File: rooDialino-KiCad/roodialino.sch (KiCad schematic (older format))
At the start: 47 parts, among them J1 Raspi Connector, J2 ICSP, J3 FTDI, J4 IR Receiver, J5 IR LED, Q1 2N7002, Q2 2N7002, Q3 2N7002, SW1 SW_Push, U1 ATmega328P, U2 TSOP312xx, U3 TXS0108EPW, Y1 16 MHz

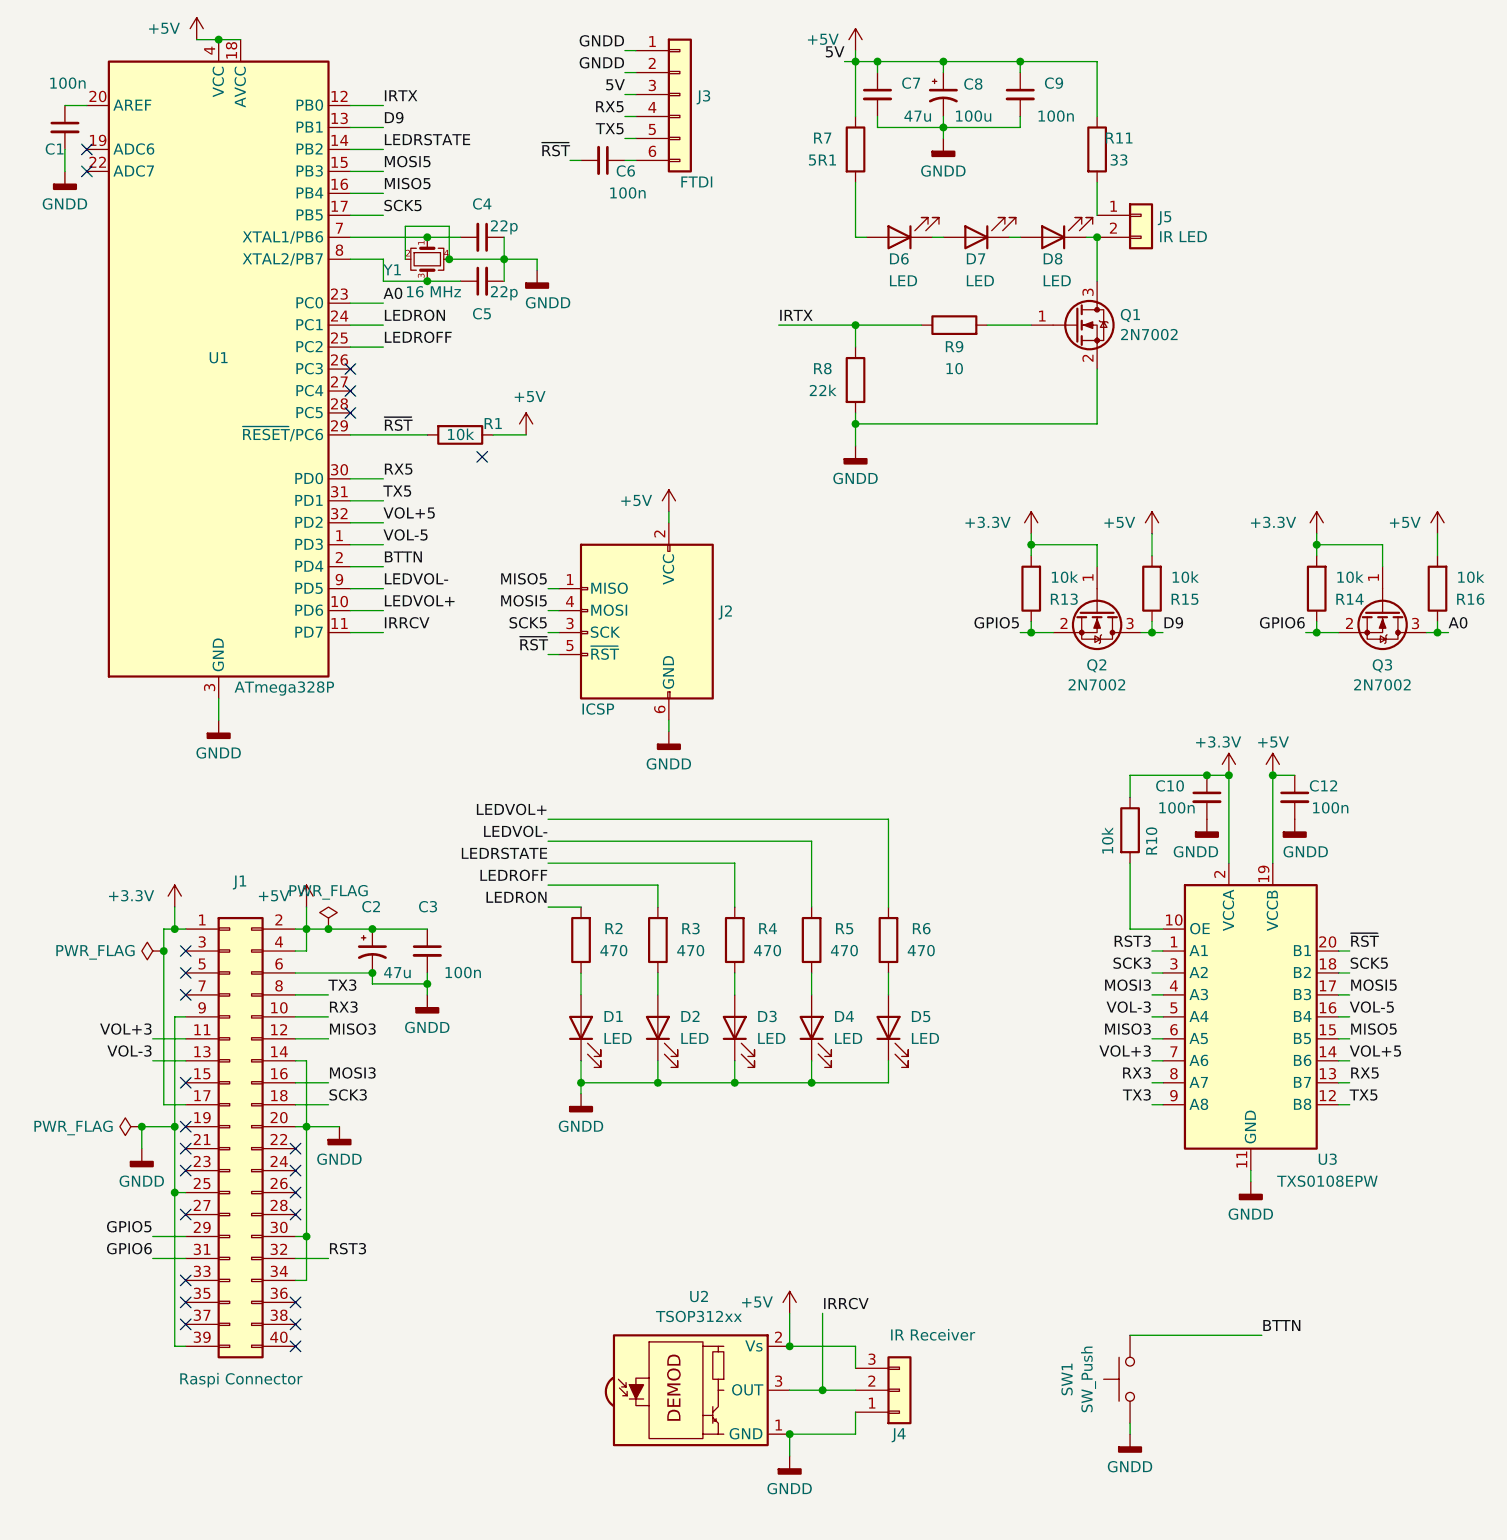
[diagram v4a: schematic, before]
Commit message: Fixing IRX wiring, adding ESO protection
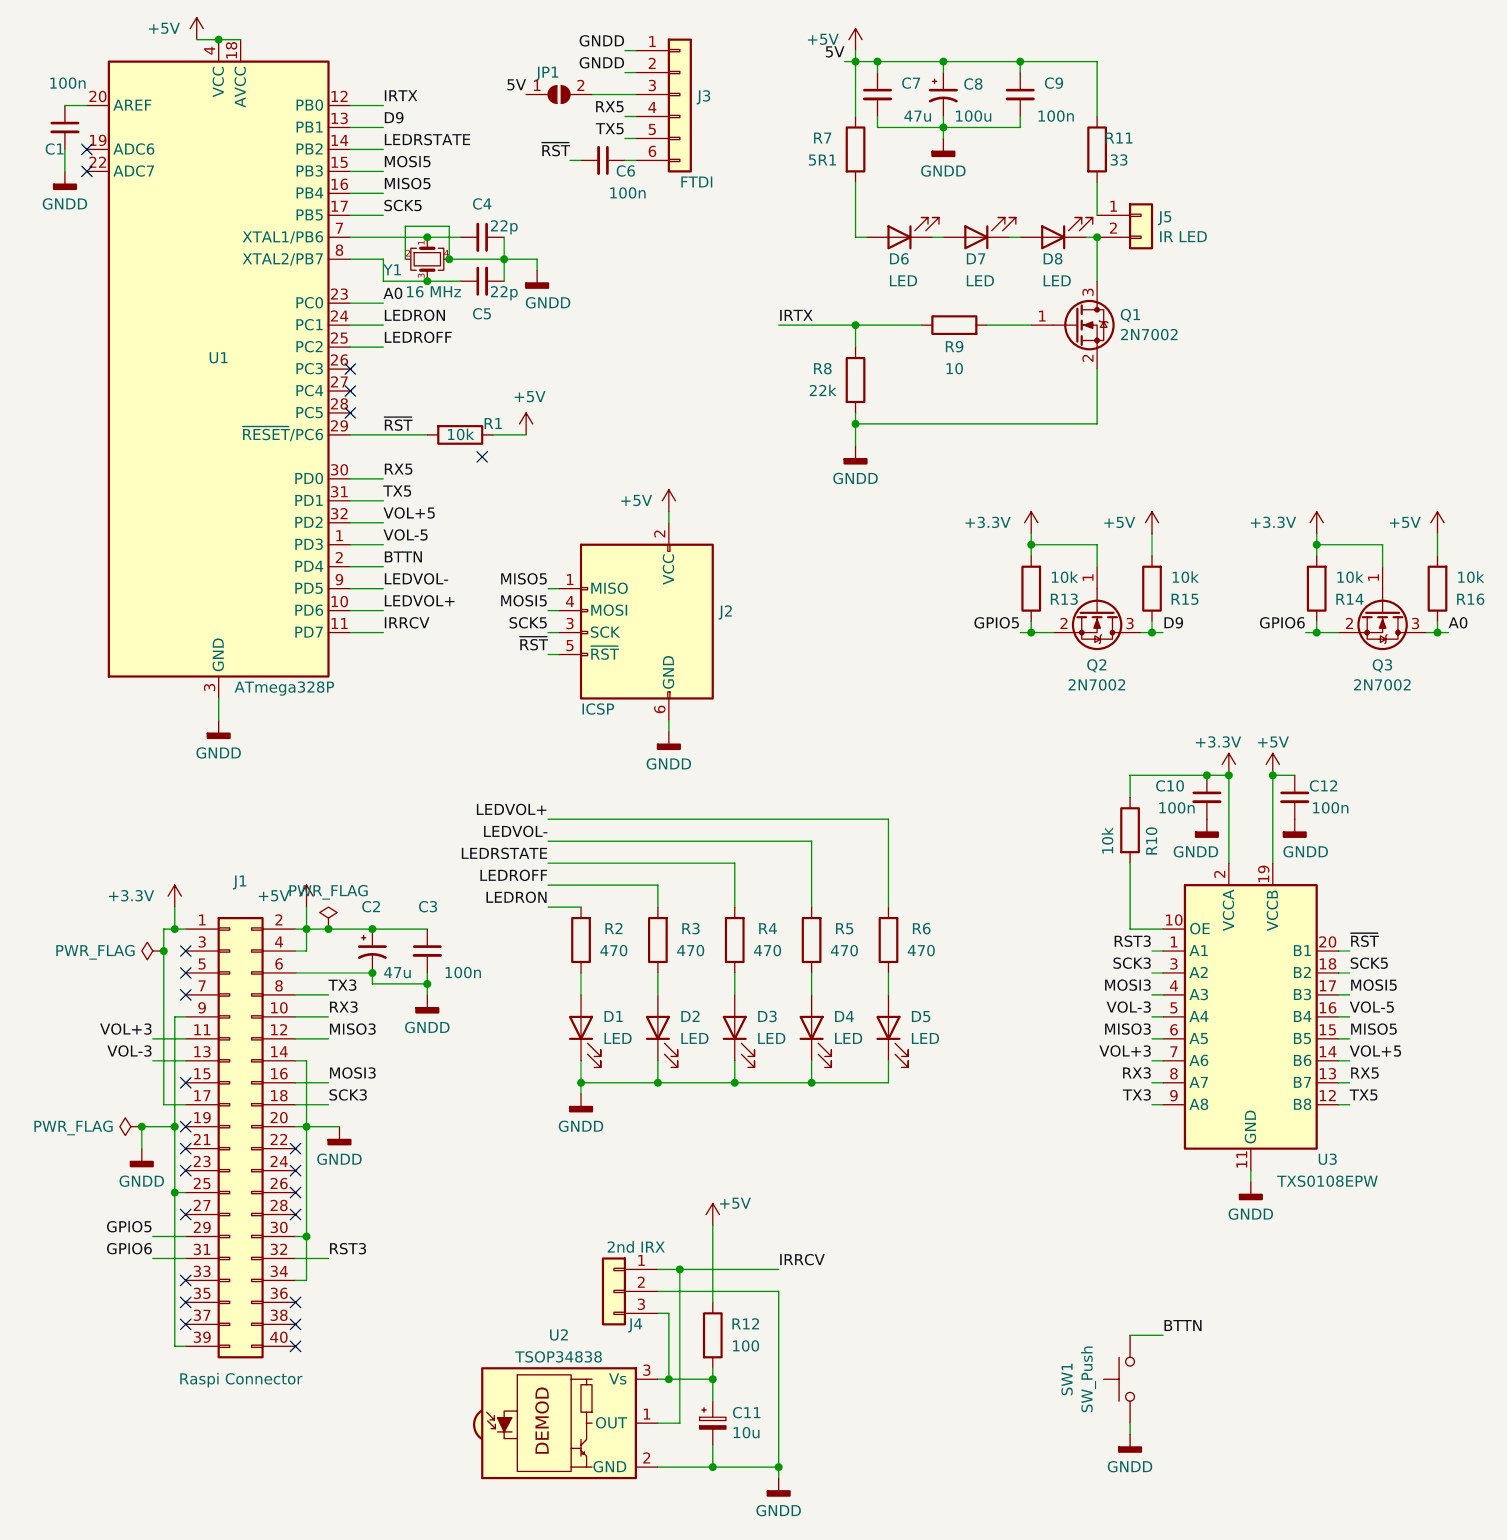
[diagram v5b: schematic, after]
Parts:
- removed U2: TSOP312xx, OptoDevice:Vishay_MINICAST-3Pin, symbol Interface_Optical:TSOP312xx
- added C11: 10u, Capacitor_Tantalum_SMD:CP_EIA-3216-18_Kemet-A, symbol Device:CP_Small
- added JP1: SolderJumper_2_Open, symbol Jumper:SolderJumper_2_Open
- added R12: 100, Resistor_SMD:R_0805_2012Metric, symbol Device:R
- added U2: TSOP34838, OptoDevice:Vishay_MOLD-3Pin, symbol Interface_Optical:TSOP348xx
- J4: value IR Receiver -> 2nd IRX
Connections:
- net +5V: now also JP1.1 (A), R12.1; no longer J3.3 (Pin_3), J4.3 (Pin_3)
- net GNDD: now also J4.2 (Pin_2), C11.2, U2.2 (GND); no longer J4.1 (Pin_1)
- net IRRCV: now also J4.1 (Pin_1), U2.1 (OUT); no longer J4.2 (Pin_2)
- new net: J3.3 (Pin_3), JP1.2 (B)
- new net: C11.1, J4.3 (Pin_3), R12.2, U2.3 (Vs)
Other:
- moved on the sheet: J4
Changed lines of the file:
@@
 Text Label 3250 950  2    50   ~ 0
 GNDD
-Text Label 3250 1050 2    50   ~ 0
+Text Label 2800 1050 2    50   ~ 0
 5V
 Text Label 3250 1150 2    50   ~ 0
@@
 	3250 1150 3300 1150
 Wire Wire Line
-	3250 1050 3300 1050
+	3100 1050 3300 1050
 Wire Wire Line
 	3250 950  3300 950
@@
 Connection ~ 5050 900
 $Comp
-L Interface_Optical:TSOP312xx U2
-U 1 1 61922DF7
-P 3600 6950
-F 0 "U2" H 3588 7375 50  0000 C CNN
-F 1 "TSOP312xx" H 3588 7284 50  0000 C CNN
-F 2 "OptoDevice:Vishay_MINICAST-3Pin" H 3550 6575 50  0001 C CNN
-F 3 "http://www.vishay.com/docs/82492/tsop312.pdf" H 4250 7250 50  0001 C CNN
-	1    3600 6950
-	1    0    0    -1
-$EndComp
-$Comp
 L power:GNDD #PWR015
 U 1 1 619248C3
-P 4000 7250
-F 0 "#PWR015" H 4000 7000 50  0001 C CNN
-F 1 "GNDD" H 4000 7100 50  0000 C CNN
-F 2 "" H 4000 7250 50  0001 C CNN
-F 3 "" H 4000 7250 50  0001 C CNN
-	1    4000 7250
-	1    0    0    -1
-$EndComp
-$Comp
-L power:+5V #PWR014
-U 1 1 6192500D
-P 4000 6600
-F 0 "#PWR014" H 4000 6450 50  0001 C CNN
-F 1 "+5V" H 3850 6650 50  0000 C CNN
-F 2 "" H 4000 6600 50  0001 C CNN
-F 3 "" H 4000 6600 50  0001 C CNN
-	1    4000 6600
-	1    0    0    -1
-$EndComp
-Wire Wire Line
-	4000 6600 4000 6750
-Wire Wire Line
-	4000 7150 4000 7250
-Text Label 4150 6600 0    50   ~ 0
+P 3950 7350
+F 0 "#PWR015" H 3950 7100 50  0001 C CNN
+F 1 "GNDD" H 3950 7200 50  0000 C CNN
+F 2 "" H 3950 7350 50  0001 C CNN
+F 3 "" H 3950 7350 50  0001 C CNN
+	1    3950 7350
+	1    0    0    -1
+$EndComp
+Text Label 3950 6400 0    50   ~ 0
 IRRCV
-Wire Wire Line
-	4300 7050 4300 7150
-Wire Wire Line
-	4300 7150 4000 7150
-Connection ~ 4000 7150
-Wire Wire Line
-	4300 6850 4300 6750
-Connection ~ 4000 6750
-Wire Wire Line
-	4000 6950 4150 6950
-Wire Wire Line
-	4000 6750 4300 6750
-Wire Wire Line
-	4150 6600 4150 6950
-Connection ~ 4150 6950
-Wire Wire Line
-	4150 6950 4300 6950
 $Comp
 L Connector_Generic:Conn_01x03 J4
 U 1 1 61933FD4
-P 4500 6950
-F 0 "J4" H 4500 7150 50  0000 C CNN
-F 1 "IR Receiver" H 4650 6700 50  0000 C CNN
-F 2 "Connector_PinHeader_2.54mm:PinHeader_1x03_P2.54mm_Vertical" H 4500 6950 50  0001 C CNN
-F 3 "~" H 4500 6950 50  0001 C CNN
-	1    4500 6950
-	1    0    0    1
+P 3200 6500
+F 0 "J4" H 3100 6350 50  0000 C CNN
+F 1 "2nd IRX" H 3100 6700 50  0000 C CNN
+F 2 "Connector_PinHeader_2.54mm:PinHeader_1x03_P2.54mm_Vertical" H 3200 6500 50  0001 C CNN
+F 3 "~" H 3200 6500 50  0001 C CNN
+	1    3200 6500
+	-1   0    0    -1
 $EndComp
 $Comp
@@
 Wire Wire Line
 	1800 5750 1950 5750
-Text Label 6150 6700 0    50   ~ 0
+Text Label 5700 6700 0    50   ~ 0
 BTTN
 Text Label 1100 6250 2    50   ~ 0
@@
 Connection ~ 2450 1800
 Wire Wire Line
-	5550 6700 6150 6700
+	5550 6700 5700 6700
 Wire Wire Line
 	5550 4250 5550 4150
@@
 	5550 4150 5900 4150
 Connection ~ 5900 4150
+$Comp
+L Jumper:SolderJumper_2_Open JP1
+U 1 1 61860523
+P 2950 1050
+F 0 "JP1" H 2900 1150 50  0000 C CNN
+F 1 "SolderJumper_2_Open" H 2950 1164 50  0001 C CNN
+F 2 "" H 2950 1050 50  0001 C CNN
+F 3 "~" H 2950 1050 50  0001 C CNN
+	1    2950 1050
+	1    0    0    -1
+$EndComp
+$Comp
+L Interface_Optical:TSOP348xx U2
+U 1 1 6174D498
+P 3000 7100
+F 0 "U2" H 2950 7500 50  0000 C CNN
+F 1 "TSOP34838" H 2950 7400 50  0000 C CNN
+F 2 "OptoDevice:Vishay_MOLD-3Pin" H 2950 6725 50  0001 C CNN
+F 3 "https://datasheet.lcsc.com/lcsc/1810171210_Vishay-Intertech-TSOP34838_C44620.pdf" H 3650 7400 50  0001 C CNN
+F 4 "C44620" H 3000 7100 50  0001 C CNN "LCSC"
+	1    3000 7100
+	1    0    0    -1
+$EndComp
+$Comp
+L Device:R R12
+U 1 1 61752F64
+P 3650 6700
+F 0 "R12" H 3800 6750 50  0000 C CNN
+F 1 "100" H 3800 6650 50  0000 C CNN
+F 2 "Resistor_SMD:R_0805_2012Metric" V 3580 6700 50  0001 C CNN
+F 3 "~" H 3650 6700 50  0001 C CNN
+F 4 "" H 3650 6700 50  0001 C CNN "LCSC"
+	1    3650 6700
+	1    0    0    -1
+$EndComp
+$Comp
+L power:+5V #PWR014
+U 1 1 6192500D
+P 3650 6200
+F 0 "#PWR014" H 3650 6050 50  0001 C CNN
+F 1 "+5V" H 3750 6300 50  0000 C CNN
+F 2 "" H 3650 6200 50  0001 C CNN
+F 3 "" H 3650 6200 50  0001 C CNN
+	1    3650 6200
+	1    0    0    -1
+$EndComp
+Wire Wire Line
+	3400 6900 3450 6900
+Wire Wire Line
+	3450 6900 3450 6600
+Wire Wire Line
+	3450 6600 3400 6600
+Wire Wire Line
+	3400 7300 3650 7300
+Wire Wire Line
+	3950 7300 3950 6500
+Wire Wire Line
+	3950 6500 3400 6500
+Wire Wire Line
+	3950 7300 3950 7350
+Connection ~ 3950 7300
+Wire Wire Line
+	3400 7100 3500 7100
+Wire Wire Line
+	3500 6400 3400 6400
+$Comp
+L Device:CP_Small C11
+U 1 1 6188FFFB
+P 3650 7100
+F 0 "C11" H 3738 7146 50  0000 L CNN
+F 1 "10u" H 3738 7055 50  0000 L CNN
+F 2 "Capacitor_Tantalum_SMD:CP_EIA-3216-18_Kemet-A" H 3650 7100 50  0001 C CNN
+F 3 "https://datasheet.lcsc.com/lcsc/1811071223_AVX-TAJA106K016RNJ_C7171.pdf" H 3650 7100 50  0001 C CNN
+F 4 "C7171" H 3650 7100 50  0001 C CNN "LCSC"
+	1    3650 7100
+	1    0    0    -1
+$EndComp
+Wire Wire Line
+	3500 6400 3500 7100
+Wire Wire Line
+	3650 7200 3650 7300
+Connection ~ 3650 7300
+Wire Wire Line
+	3650 7300 3950 7300
+Wire Wire Line
+	3650 7000 3650 6900
+Wire Wire Line
+	3650 6900 3450 6900
+Connection ~ 3450 6900
+Wire Wire Line
+	3650 6900 3650 6850
+Connection ~ 3650 6900
+Wire Wire Line
+	3500 6400 3950 6400
+Connection ~ 3500 6400
+Wire Wire Line
+	3650 6200 3650 6550
 $EndSCHEMATC

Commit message: Saving before i size down some 0805s
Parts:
- JP1: footprint (none) -> Jumper:SolderJumper-2_P1.3mm_Open_RoundedPad1.0x1.5mm
- R12: footprint Resistor_SMD:R_0805_2012Metric -> Resistor_SMD:R_0603_1608Metric; LCSC (none) -> C2275
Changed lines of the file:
@@
 F 0 "JP1" H 2900 1150 50  0000 C CNN
 F 1 "SolderJumper_2_Open" H 2950 1164 50  0001 C CNN
-F 2 "" H 2950 1050 50  0001 C CNN
+F 2 "Jumper:SolderJumper-2_P1.3mm_Open_RoundedPad1.0x1.5mm" H 2950 1050 50  0001 C CNN
 F 3 "~" H 2950 1050 50  0001 C CNN
 	1    2950 1050
@@
 F 0 "R12" H 3800 6750 50  0000 C CNN
 F 1 "100" H 3800 6650 50  0000 C CNN
-F 2 "Resistor_SMD:R_0805_2012Metric" V 3580 6700 50  0001 C CNN
+F 2 "Resistor_SMD:R_0603_1608Metric" V 3580 6700 50  0001 C CNN
 F 3 "~" H 3650 6700 50  0001 C CNN
-F 4 "" H 3650 6700 50  0001 C CNN "LCSC"
+F 4 "C2275" H 3650 6700 50  0001 C CNN "LCSC"
 	1    3650 6700
 	1    0    0    -1
